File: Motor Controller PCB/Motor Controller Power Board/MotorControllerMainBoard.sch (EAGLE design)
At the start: 43 parts

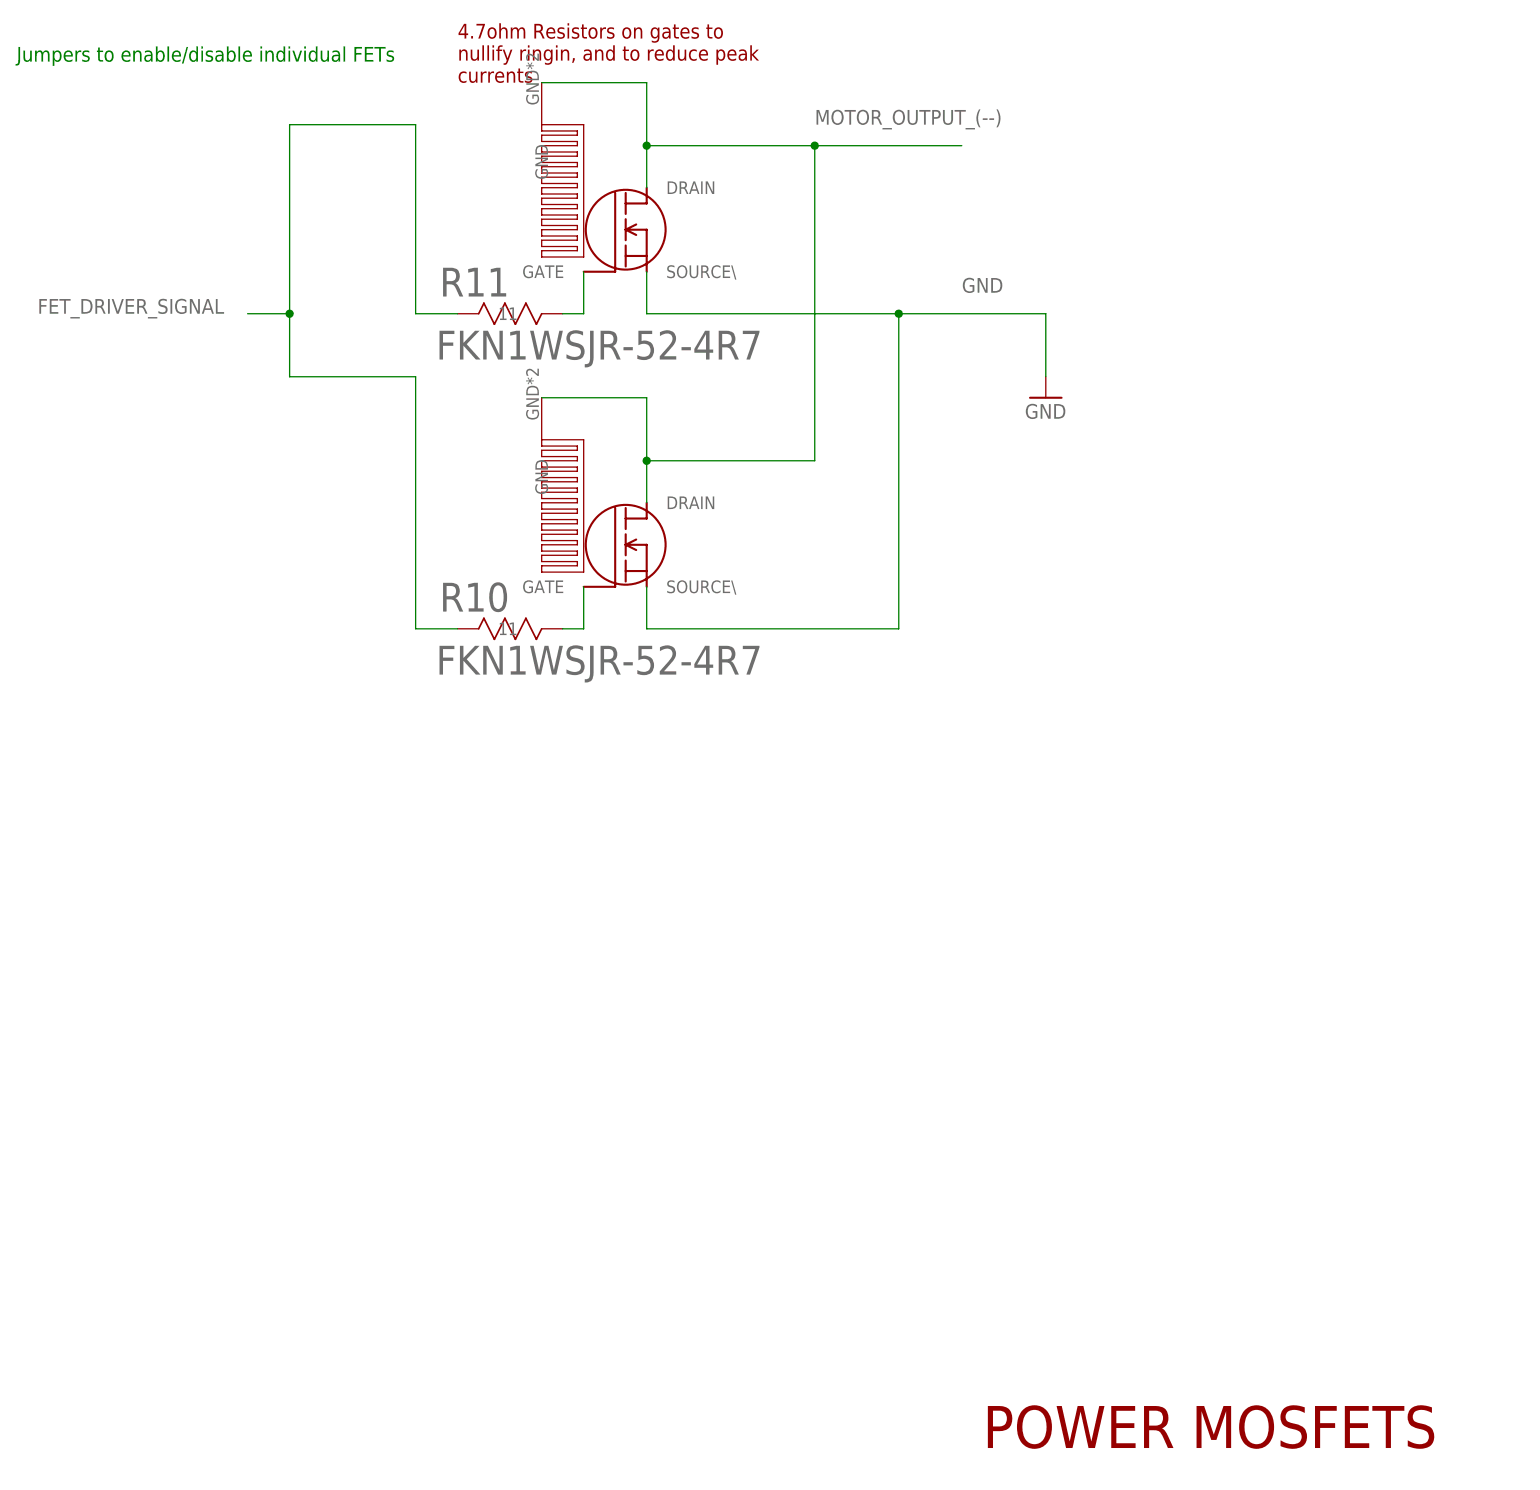
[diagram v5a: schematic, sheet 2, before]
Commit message: added TVS diodes and text
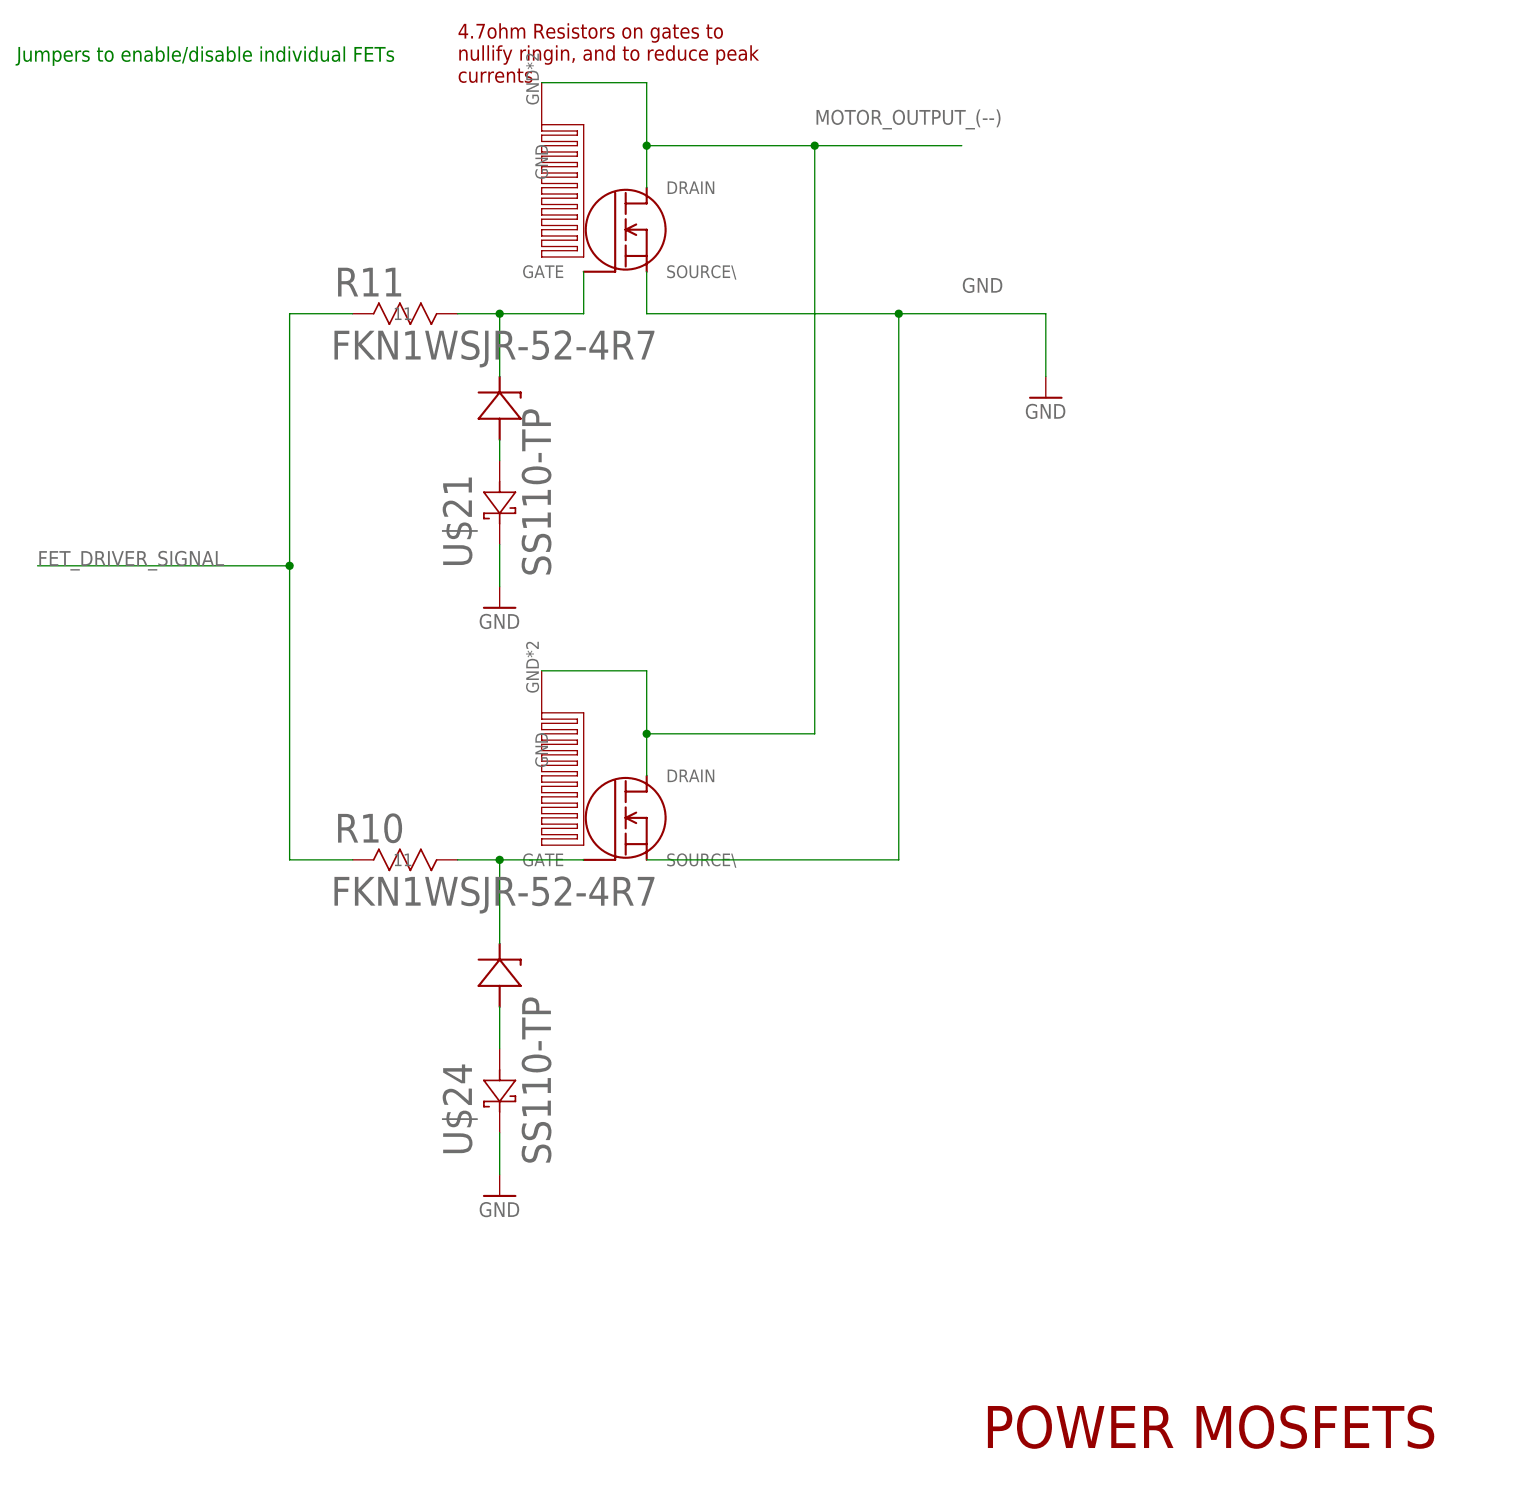
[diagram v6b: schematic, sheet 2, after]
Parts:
- removed SV8: (no value), con-lstb:MA04-1
- added SV2: (no value), con-lstb:MA03-1
- added U$20, U$7: SMBJ15CD, MotorControllerEagleLibrary:SMBJ15CD
- added U$21, U$24: SS110-TP, MotorControllerEagleLibrary:SS110-TP
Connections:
- new net N$1: U$24.ANODE, U$7.ANODE
- new net N$4: U$20.ANODE, U$21.ANODE
- net 12V_POWER_REGULATED: now also SV2.1; no longer SV8.2
- net FET_DRIVER_SIGNAL: now also SV2.2; no longer SV8.3
- net GND: now also SV2.3, U$21.CATHODE, U$24.CATHODE; no longer SV8.4
- net MOTOR_OUTPUT_(+): no longer SV8.1
- net N$10: now also U$20.CATHODE
- net N$2: now also U$7.CATHODE
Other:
- moved on the sheet: R10, R11
